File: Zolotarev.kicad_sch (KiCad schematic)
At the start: 205 parts, among them J1 RF_IN, J2 RF_OUT, K1 G5LE-1, K10 G5LE-1, K11 G5LE-1, K13 G5LE-1, K14 G5LE-1, K15 G5LE-1, K2 G5LE-1, K3 G5LE-1, K4 G5LE-1, K5 G5LE-1, K6 G5LE-1, K7 G5LE-1, K8 G5LE-1, K9 G5LE-1

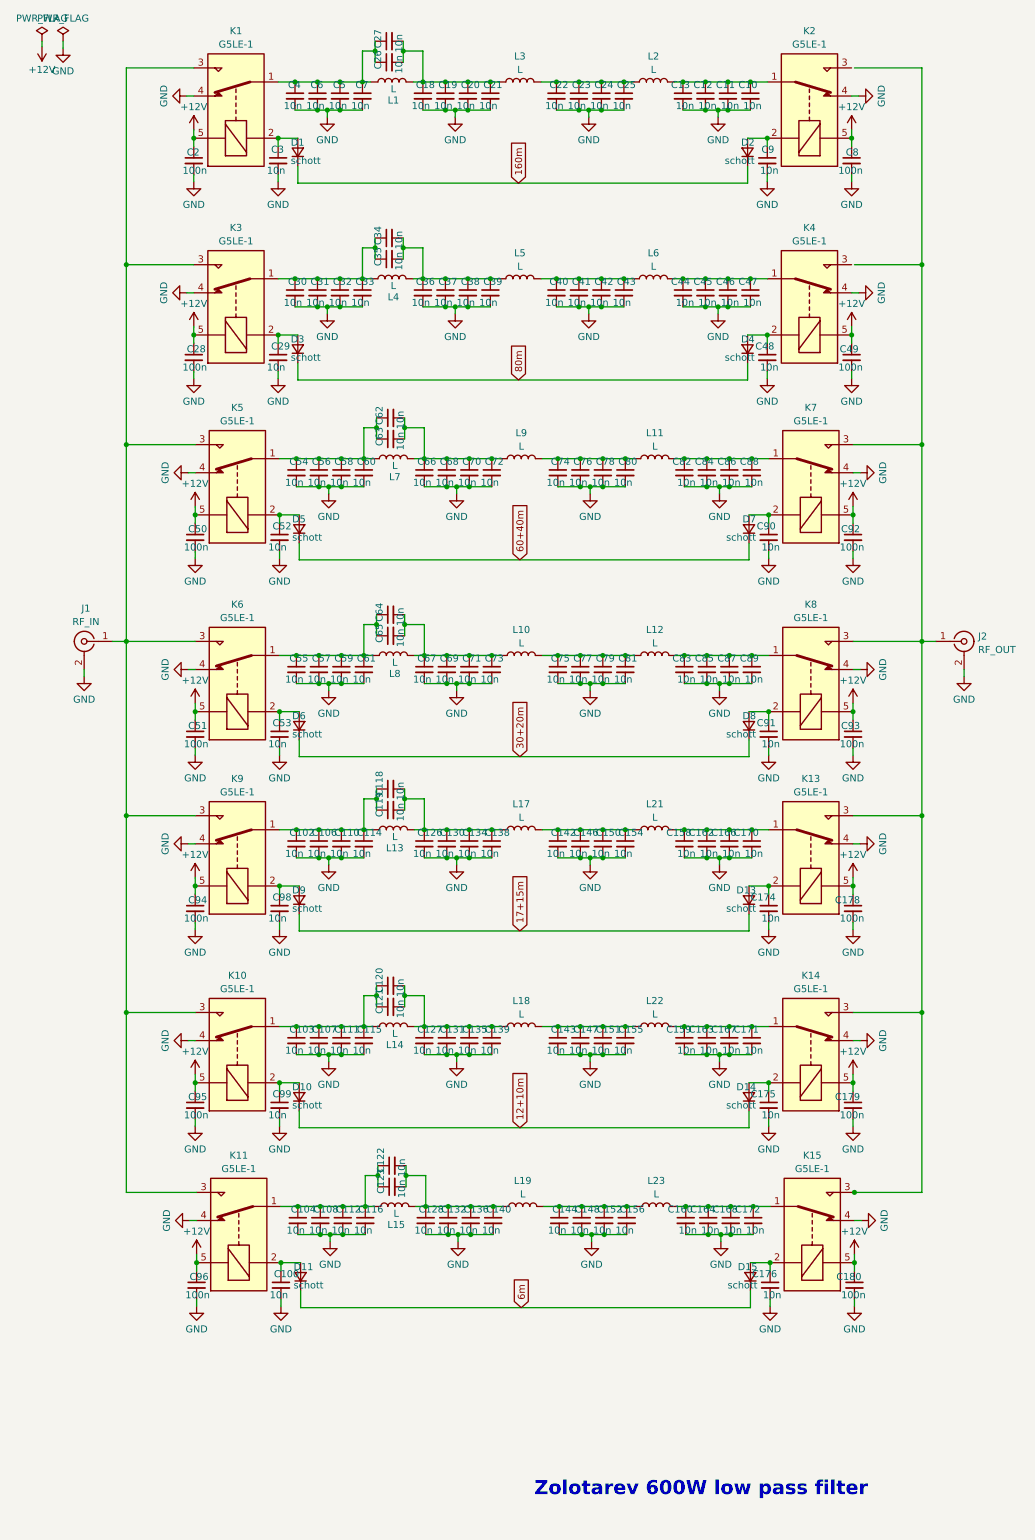
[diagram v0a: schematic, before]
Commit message: schematic completed, devices def TBD
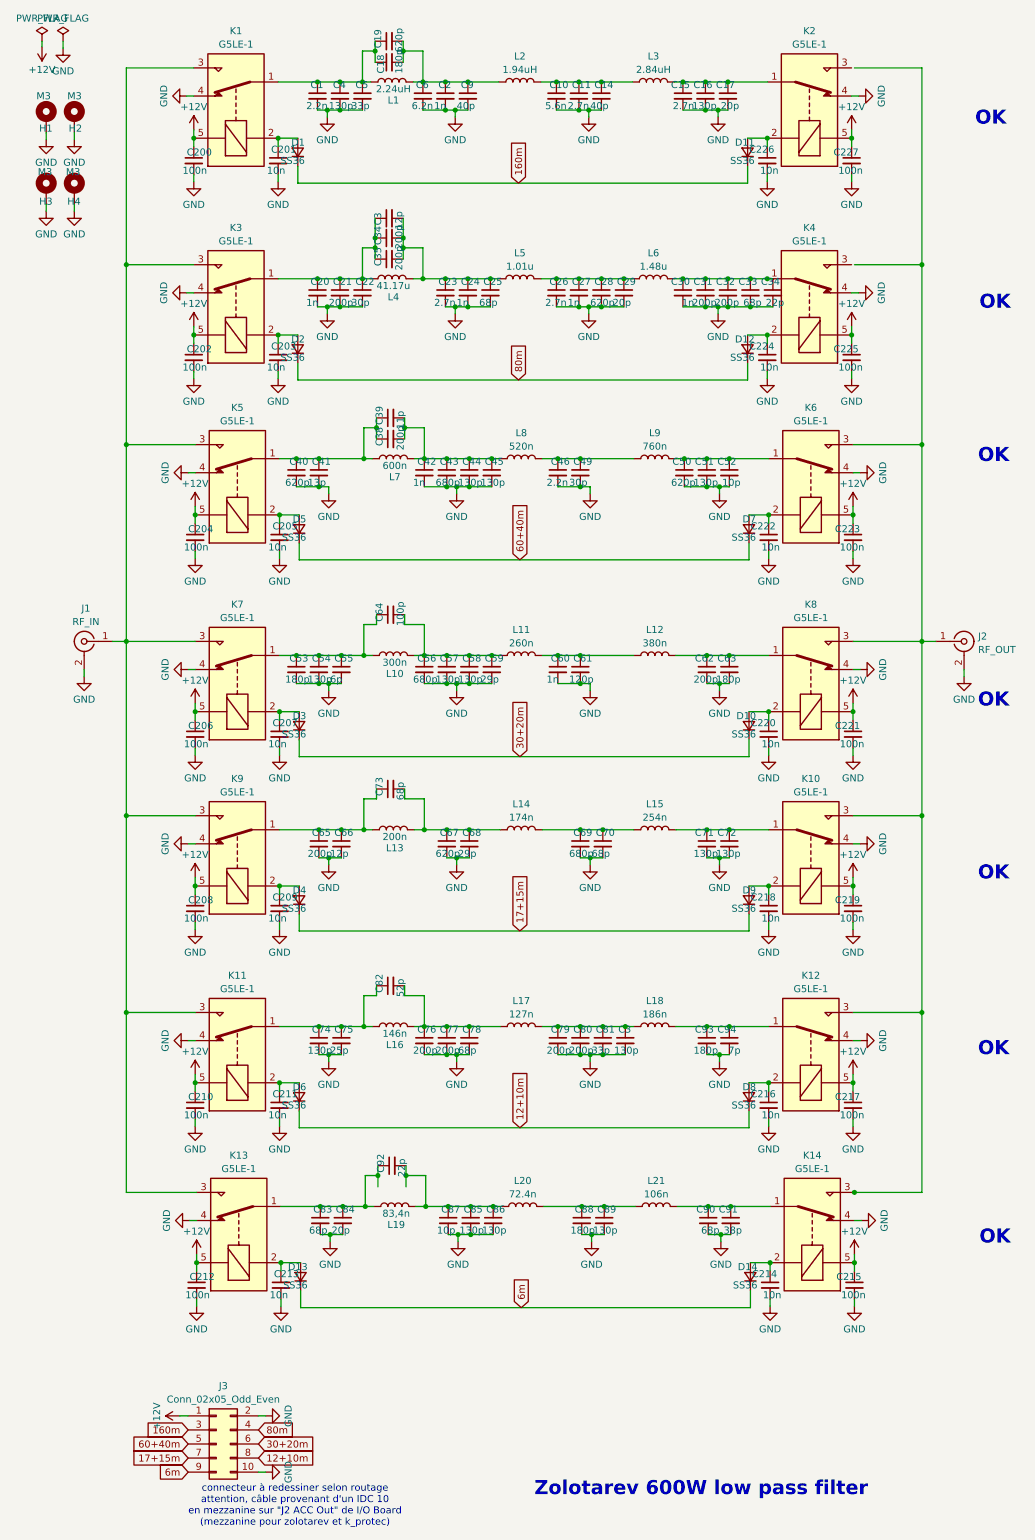
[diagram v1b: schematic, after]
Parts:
- removed C10, C102, C103, C104, C114, C115, C116, C119, C121, C123, C126, C128, C138, C139, C142, C144, C154, C156, C158, C159, C160, C170, C171, C172, C21, C25, C30, C36, C4, C58, C60, C61, C65, C78, C79, C80, C81, C83, C88, C89: 10n, symbol Device:C_Small
- removed D15: schott, symbol Device:D_Small
- added C3: 12p, symbol Device:C_Small
- added C34: 22p, symbol Device:C_Small
- added D12: SS36, Diode_SMD:D_SMC, symbol Device:D_Small
- added H1, H2, H3, H4: M3, MountingHole:MountingHole_3.5mm_Pad_Via, symbol Mechanical:MountingHole_Pad
- added J3: Conn_02x05_Odd_Even, symbol Connector_Generic:Conn_02x05_Odd_Even
- C1: renamed from C6; value 10n -> 2.2n
- C10: renamed from C22; value 10n -> 5.6n
- C11: renamed from C23; value 10n -> 2.7n
- C14: renamed from C24; value 10n -> 40p
- C15: renamed from C13; value 10n -> 2.7n
- C16: renamed from C12; value 10n -> 130p
- C17: renamed from C11; value 10n -> 20p
- C18: renamed from C26; value 10n -> 180p
- C19: renamed from C27; value 10n -> 620p
- C2: renamed from C19; value 10n -> 1n
- C20: renamed from C31; value 10n -> 1n
- C21: renamed from C32; value 10n -> 200p
- C22: renamed from C33; value 10n -> 30p
- C23: renamed from C37; value 10n -> 2.7n
- C24: renamed from C38; value 10n -> 1n
- C25: renamed from C39; value 10n -> 68p
- C26: renamed from C40; value 10n -> 2.7n
- C27: renamed from C41; value 10n -> 1n
- C28: renamed from C42; value 10n -> 620p
- C29: renamed from C43; value 10n -> 20p
- C3: renamed from C155; value 10n -> 130p
- C30: renamed from C44; value 10n -> 1n
- C31: renamed from C45; value 10n -> 200p
- C32: renamed from C46; value 10n -> 200p
- C33: renamed from C47; value 10n -> 68p
- C34, C35: value 10n -> 200p
- C38: renamed from C63; value 10n -> 200p
- C39: renamed from C62; value 10n -> 11p
- C4: renamed from C5; value 10n -> 130p
- C40: renamed from C54; value 10n -> 620p
- C41: renamed from C56; value 10n -> 13p
- C42: renamed from C66; value 10n -> 1n
- C43: renamed from C68; value 10n -> 680p
- C44: renamed from C70; value 10n -> 130p
- C45: renamed from C72; value 10n -> 130p
- C46: renamed from C74; value 10n -> 2.2n
- C49: renamed from C76; value 10n -> 30p
- C5: renamed from C7; value 10n -> 33p
- C50: renamed from C82; value 10n -> 620p
- C51: renamed from C84; value 10n -> 130p
- C52: renamed from C86; value 10n -> 10p
- C53: renamed from C55; value 10n -> 180p
- C54: renamed from C57; value 10n -> 130p
- C55: renamed from C59; value 10n -> 6p
- C56: renamed from C67; value 10n -> 680p
- C57: renamed from C69; value 10n -> 130p
- C58: renamed from C71; value 10n -> 130p
- C59: renamed from C73; value 10n -> 29p
- C6: renamed from C18; value 10n -> 6.2n
- C60: renamed from C75; value 10n -> 1n
- C61: renamed from C77; value 10n -> 120p
- C62: renamed from C85; value 10n -> 200p
- C63: renamed from C87; value 10n -> 180p
- C64: value 10n -> 100p
- C65: renamed from C106; value 10n -> 200p
- C66: renamed from C110; value 10n -> 12p
- C67: renamed from C130; value 10n -> 620p
- C68: renamed from C134; value 10n -> 29p
- C69: renamed from C146; value 10n -> 680p
- C70: renamed from C150; value 10n -> 68p
- C71: renamed from C162; value 10n -> 130p
- C72: renamed from C166; value 10n -> 130p
- C73: renamed from C118; value 10n -> 68p
- C74: renamed from C107; value 10n -> 130p
- C75: renamed from C111; value 10n -> 25p
- C76: renamed from C127; value 10n -> 200p
- C77: renamed from C131; value 10n -> 200p
- C78: renamed from C135; value 10n -> 68p
- C79: renamed from C143; value 10n -> 200p
- C80: renamed from C147; value 10n -> 200p
- C81: renamed from C151; value 10n -> 33p
- C82: renamed from C120; value 10n -> 52p
- C83: renamed from C108; value 10n -> 68p
- C84: renamed from C112; value 10n -> 20p
- C85: renamed from C136; value 10n -> 130p
- C86: renamed from C140; value 10n -> 130p
- C87: renamed from C132; value 10n -> 10p
- C88: renamed from C148; value 10n -> 180p
- C89: renamed from C152; value 10n -> 130p
- C9: renamed from C20; value 10n -> 40p
- C90: renamed from C164; value 10n -> 68p
- C91: renamed from C168; value 10n -> 38p
- C92: renamed from C122; value 10n -> 22p
- C93: renamed from C163; value 10n -> 180p
- C94: renamed from C167; value 10n -> 7p
- D1, D10, D11, D13, D14, D2, D3, D4, D5, D6, D7, D8, D9: value schott -> SS36; footprint (none) -> Diode_SMD:D_SMC
- L1: value L -> 2.24uH
- L10: renamed from L8; value L -> 300n
- L11: renamed from L10; value L -> 260n
- L12: value L -> 380n
- L13: value L -> 200n
- L14: renamed from L17; value L -> 174n
- L15: renamed from L21; value L -> 254n
- L16: renamed from L14; value L -> 146n
- L17: renamed from L18; value L -> 127n
- L18: renamed from L22; value L -> 186n
- L19: renamed from L15; value L -> 83,4n
- L2: renamed from L3; value L -> 1.94uH
- L20: renamed from L19; value L -> 72.4n
- L21: renamed from L23; value L -> 106n
- L3: renamed from L2; value L -> 2.84uH
- L4: value L -> 41.17u
- L5: value L -> 1.01u
- L6: value L -> 1.48u
- L7: value L -> 600n
- L8: renamed from L9; value L -> 520n
- L9: renamed from L11; value L -> 760n
- renumbered C2 to C200, C3 to C201, C28 to C202, C29 to C203, C50 to C204, C52 to C205, C51 to C206, C53 to C207, C94 to C208, C98 to C209, C95 to C210, C99 to C211, C96 to C212, C100 to C213, C176 to C214, C180 to C215, C175 to C216, C179 to C217, C174 to C218, C178 to C219, C91 to C220, C93 to C221, C90 to C222, C92 to C223, C48 to C224, C49 to C225, C9 to C226, C8 to C227, K13 to K10, K10 to K11, K14 to K12, K11 to K13, K15 to K14, K7 to K6, K6 to K7
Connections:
- net +12V: now also J3.1 (Pin_1)
- net 12+10m: now also D6.1 (K), D8.1 (K), J3.8 (Pin_8); no longer D10.1 (K), D14.1 (K)
- net 160m: now also D11.1 (K), J3.3 (Pin_3); no longer D2.1 (K)
- net 17+15m: now also D4.1 (K), J3.7 (Pin_7); no longer D13.1 (K)
- net 30+20m: now also D10.1 (K), D3.1 (K), J3.6 (Pin_6); no longer D6.1 (K), D8.1 (K)
- net 60+40m: now also J3.5 (Pin_5)
- net 6m: now also D13.1 (K), D14.1 (K), J3.9 (Pin_9); no longer D11.1 (K)
- net 80m: now also D2.1 (K), D12.1 (K), J3.4 (Pin_4); no longer D3.1 (K), D4.1 (K)
- net GND: now also C34.2, H1.1, H2.1, H3.1, H4.1, J3.10 (Pin_10), J3.2 (Pin_2)
- net at C20.1, C21.1, C22.1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: now also C3.1
- net at C207.1, K7.2: now also D3.2 (A); no longer D6.2 (A)
- net at C203.1, K3.2: now also D2.2 (A); no longer D3.2 (A)
- net at C216.1, K12.2: now also D8.2 (A); no longer D14.2 (A)
- net at C214.1, K14.2: now also D14.2 (A)
- net at C23.1, C24.1, C25.1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: now also C3.2
- net at C209.1, K9.2: now also D4.2 (A); no longer D9.2 (A)
- net at C224.1, K4.2: now also D12.2 (A); no longer D4.2 (A)
- net at C218.1, K10.2: now also D9.2 (A); no longer D13.2 (A)
- net at C226.1, K2.2: now also D11.2 (A); no longer D2.2 (A)
- net at C213.1, K13.2: now also D13.2 (A); no longer D11.2 (A)
- net at C30.1, C31.1, C32.1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: now also C34.1
- net at C220.1, K8.2: now also D10.2 (A); no longer D8.2 (A)
- net at C211.1, K11.2: now also D6.2 (A); no longer D10.2 (A)
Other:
- note added: "OK"
- note added: "connecteur à redessiner selon routage attention, câble provenant d'un IDC 10 en mezzanine sur "J2 ACC Out" de I/O Board (mezzanine pour zolotarev et k_protec)"

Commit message: beginning to assign 3D forms
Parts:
- C1: footprint (none) -> ATC_B:ATC_500_HandSoldering
- C200, C201, C202, C203, C204, C205, C206, C207, C208, C209, C210, C211, C212, C213, C214, C215, C216, C217, C218, C219, C220, C221, C222, C223, C224, C225, C226, C227: footprint (none) -> Capacitor_SMD:C_0805_2012Metric_Pad1.18x1.45mm_HandSolder
- C3: value 130p -> 33p
- C81: value 33p -> 130p
- L1, L10, L11, L12, L13, L14, L15, L2, L3, L4, L5, L6, L7, L8, L9: footprint (none) -> T80_60_V:T60_80_V
- L16, L17, L18, L19, L20, L21: footprint (none) -> T80_60_V:Air_Coil
- renumbered C34 to C36, C3 to C37
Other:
- note added: "Manque ferrites filtrage DC"

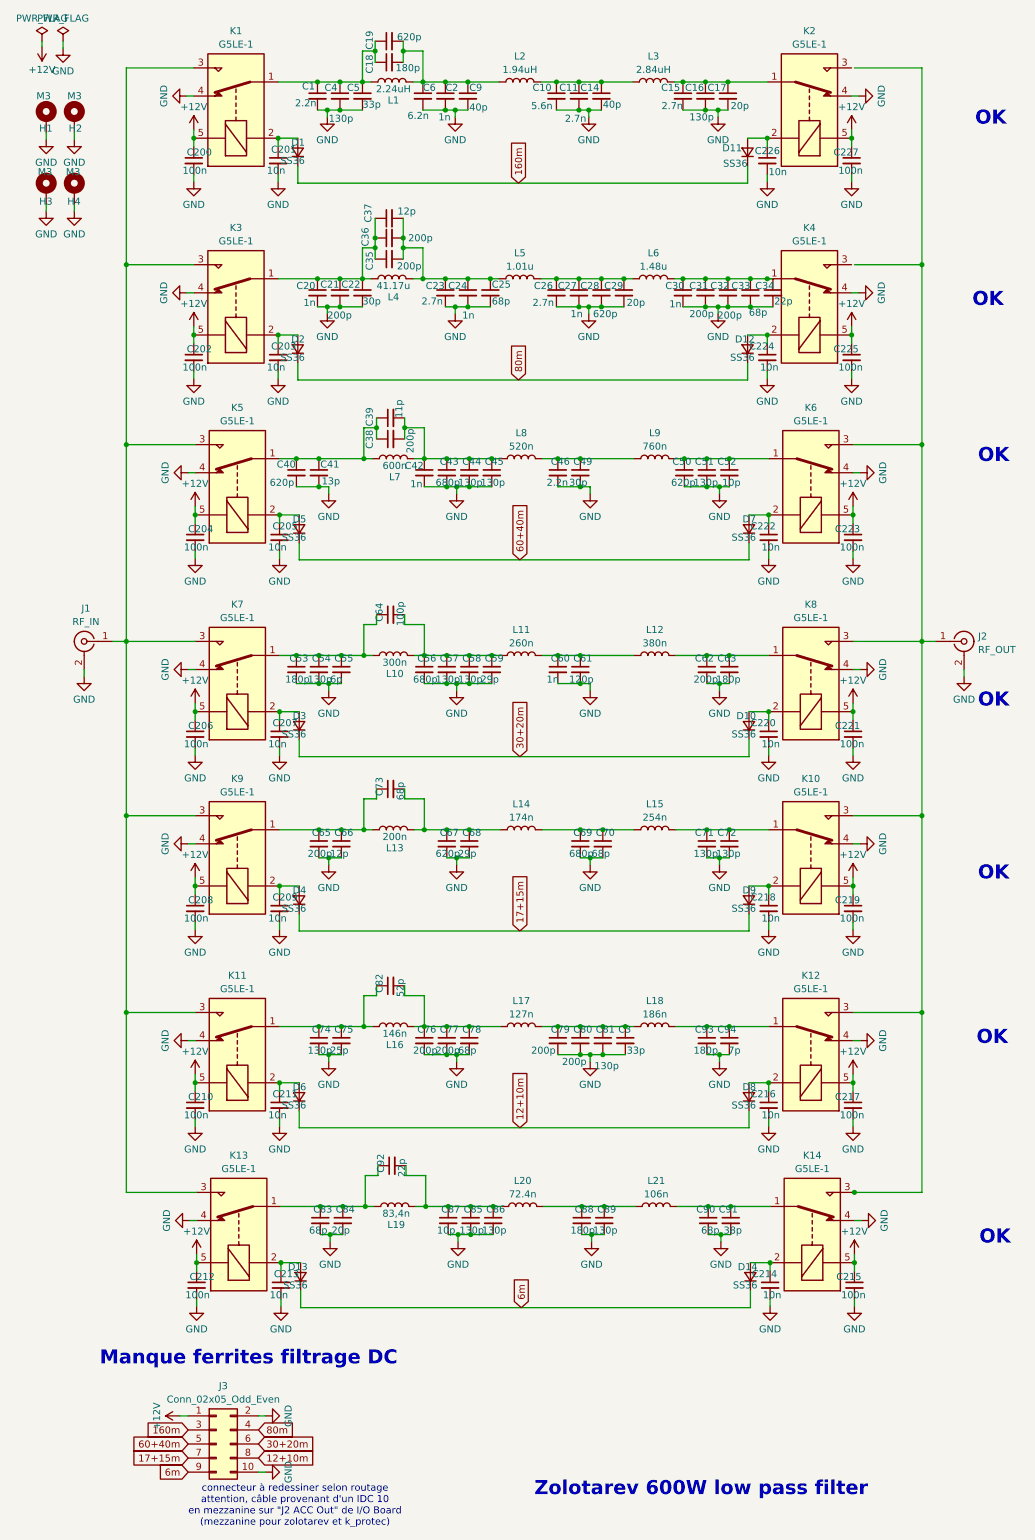
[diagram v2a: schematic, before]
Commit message: minor corrections, first band routed
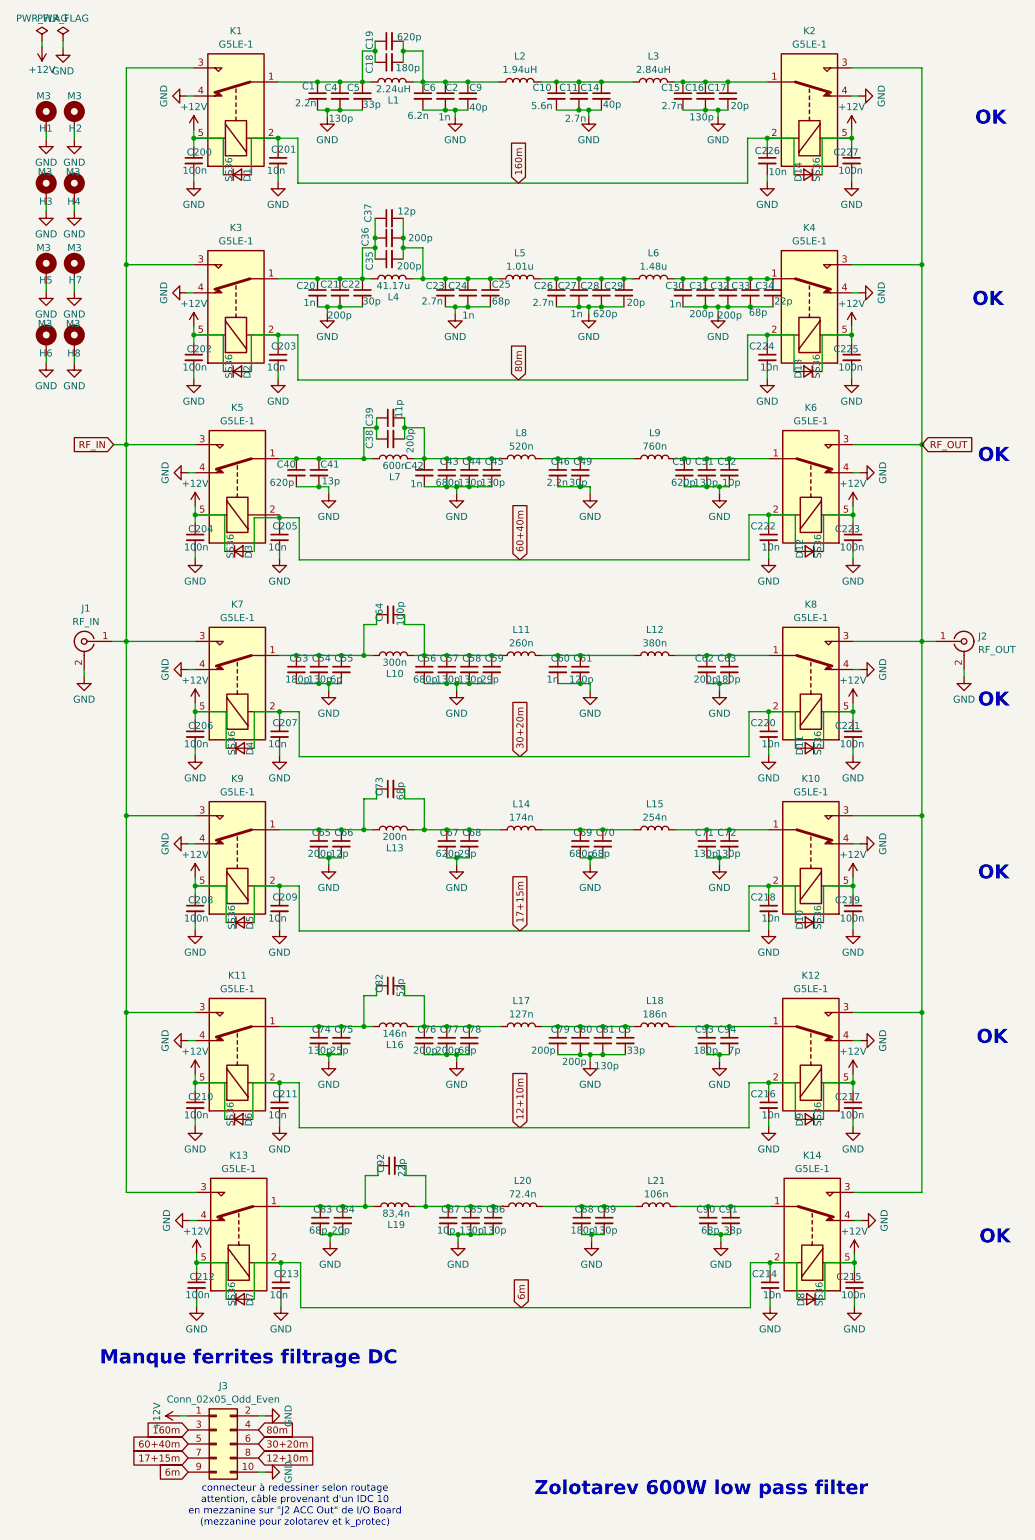
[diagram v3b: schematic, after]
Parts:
- added H5, H6, H7, H8: M3, MountingHole:MountingHole_3.5mm_Pad_Via, symbol Mechanical:MountingHole_Pad
- C10, C11, C14, C15, C16, C17, C18, C19, C2, C20, C21, C22, C23, C24, C25, C26, C27, C28, C29, C3, C30, C31, C32, C33, C34, C35, C36, C37, C38, C39, C4, C40, C41, C42, C43, C44, C45, C46, C49, C5, C50, C51, C52, C53, C54, C55, C56, C57, C58, C59, C6, C60, C61, C62, C63, C64, C65, C66, C67, C68, C69, C70, C71, C72, C73, C74, C75, C76, C77, C78, C79, C80, C81, C82, C83, C84, C85, C86, C87, C88, C89, C9, C90, C91, C92, C93, C94: footprint (none) -> ATC_B:ATC_500_HandSoldering
- J1, J2: footprint (none) -> SMA_PINS:SMA_PINS
- J3: footprint (none) -> Connector_IDC:IDC-Header_2x05_P2.54mm_Vertical
- L1, L10, L11, L12, L13, L14, L15, L2, L3, L4, L5, L6, L7, L8, L9: footprint T80_60_V:T60_80_V -> T80_60_V:T90_60_V
- L16, L17, L18, L19, L20, L21: footprint T80_60_V:Air_Coil -> T80_60_V:Large_Air_Coil
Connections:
- net +12V: now also D1.1 (K), D10.1 (K), D11.1 (K), D12.1 (K), D13.1 (K), D14.1 (K), D2.1 (K), D3.1 (K), D6.1 (K), D7.1 (K), D8.1 (K), D9.1 (K)
- net 12+10m: now also C211.1, C216.1, D6.2 (A), D9.2 (A), K11.2, K12.2; no longer D6.1 (K), D8.1 (K)
- net 160m: now also C201.1, C226.1, D1.2 (A), D14.2 (A), K1.2, K2.2; no longer D1.1 (K), D11.1 (K)
- net 17+15m: now also C209.1, C218.1, D10.2 (A), D5.2 (A), K10.2, K9.2; no longer D4.1 (K), D9.1 (K)
- net 30+20m: now also C207.1, C220.1, D11.2 (A), D4.2 (A), K7.2, K8.2; no longer D10.1 (K), D3.1 (K)
- net 60+40m: now also C205.1, C222.1, D12.2 (A), K5.2, K6.2; no longer D5.1 (K), D7.1 (K)
- net 6m: now also C213.1, C214.1, D7.2 (A), D8.2 (A), K13.2, K14.2; no longer D13.1 (K), D14.1 (K)
- net 80m: now also C203.1, C224.1, D13.2 (A), D2.2 (A), K3.2, K4.2; no longer D12.1 (K), D2.1 (K)
- net GND: now also H5.1, H6.1, H7.1, H8.1
- net RF_OUT: now reaches J2.1 (In), K10.3, K12.3, K14.3, K6.3, K8.3
- net RF_OUT: now also K2.3, K4.3
- net RF_IN: now reaches J1.1 (In), K1.3, K11.3, K13.3, K3.3, K5.3, K7.3, K9.3
- now unconnected: D3.2 (A)
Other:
- moved on the sheet: D1

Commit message: 3 bands over 7
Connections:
- net 60+40m: now also D3.2 (A)
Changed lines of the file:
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@@
+	(wire
+		(pts
+			(xy 51.816 107.188) (xy 52.07 107.188)
+		)
+		(stroke
+			(width 0)
+			(type default)
+		)
+	)
 	(wire
 		(pts
